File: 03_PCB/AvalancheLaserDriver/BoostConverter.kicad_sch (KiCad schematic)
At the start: 24 parts, among them IC1 LT8365JMSE, SW1 JS202011JAQN

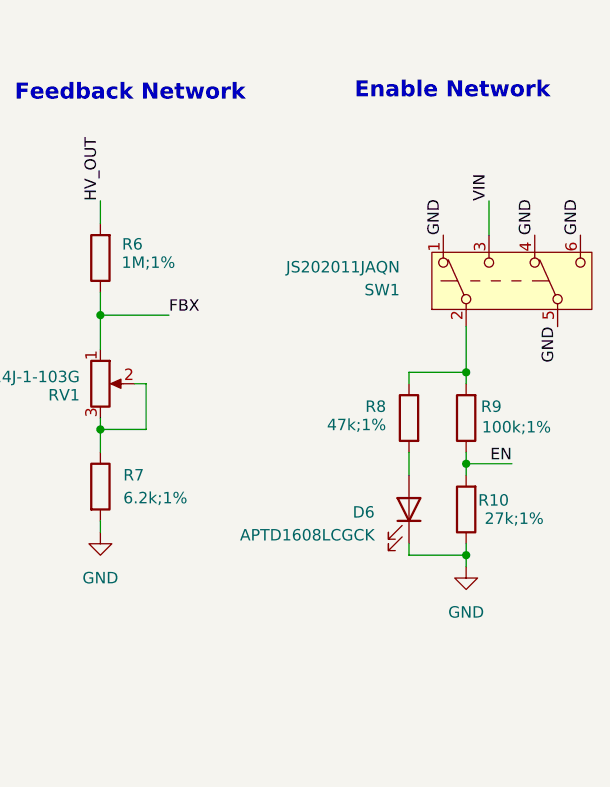
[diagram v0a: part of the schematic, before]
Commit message: feat(pcb): update laser driver circuit after first iteration
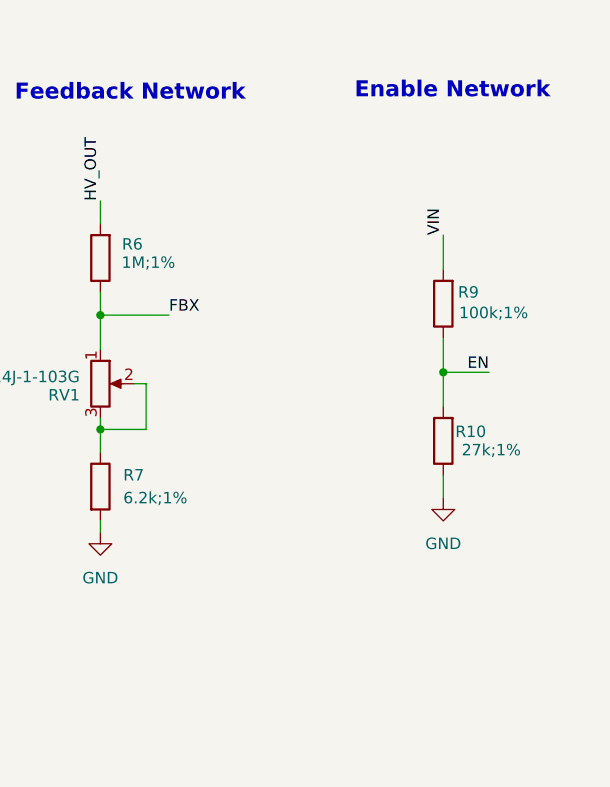
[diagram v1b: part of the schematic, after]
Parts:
- removed D6: APTD1608LCGCK, LED_SMD:LED_0603_1608Metric, symbol Device:LED
- removed R8: 47k;1%, Resistor_SMD:R_0603_1608Metric, symbol Device:R
- removed SW1: JS202011JAQN, Button_Switch_SMD:SW_DPDT_CK_JS202011JCQN, symbol Switch:SW_Push_DPDT
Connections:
- net VIN: now also R9.2
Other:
- moved on the sheet: R10, R9

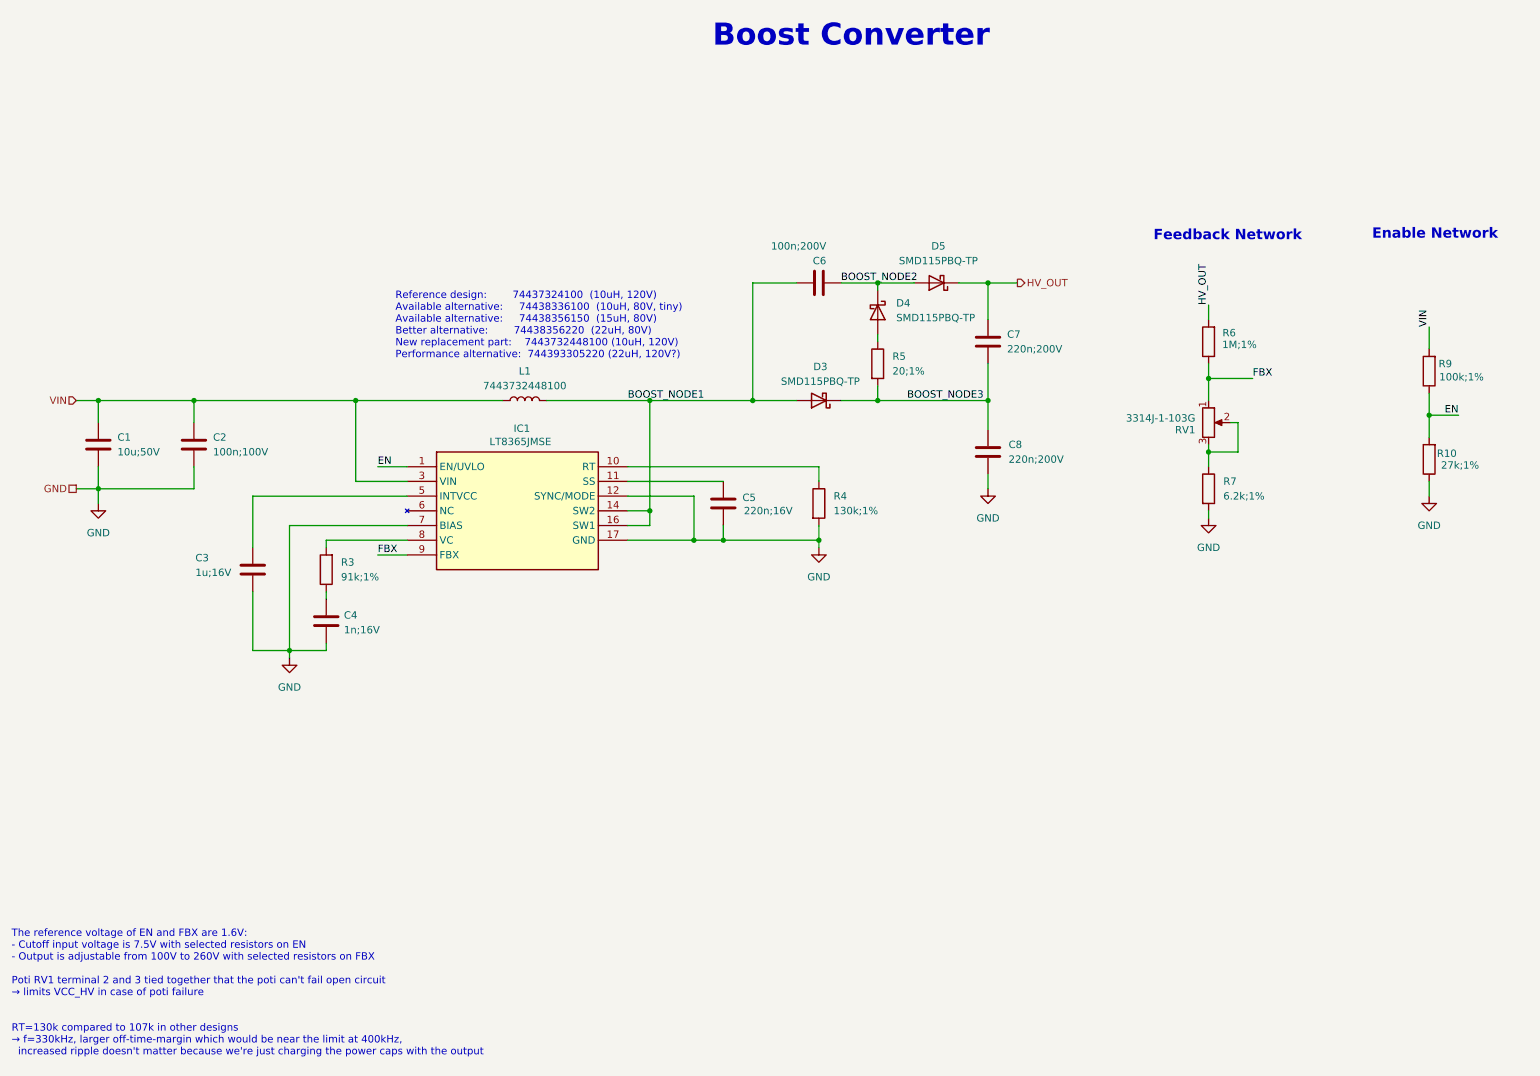
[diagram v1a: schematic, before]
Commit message: feat(pcb): Increase operating voltage to 320V
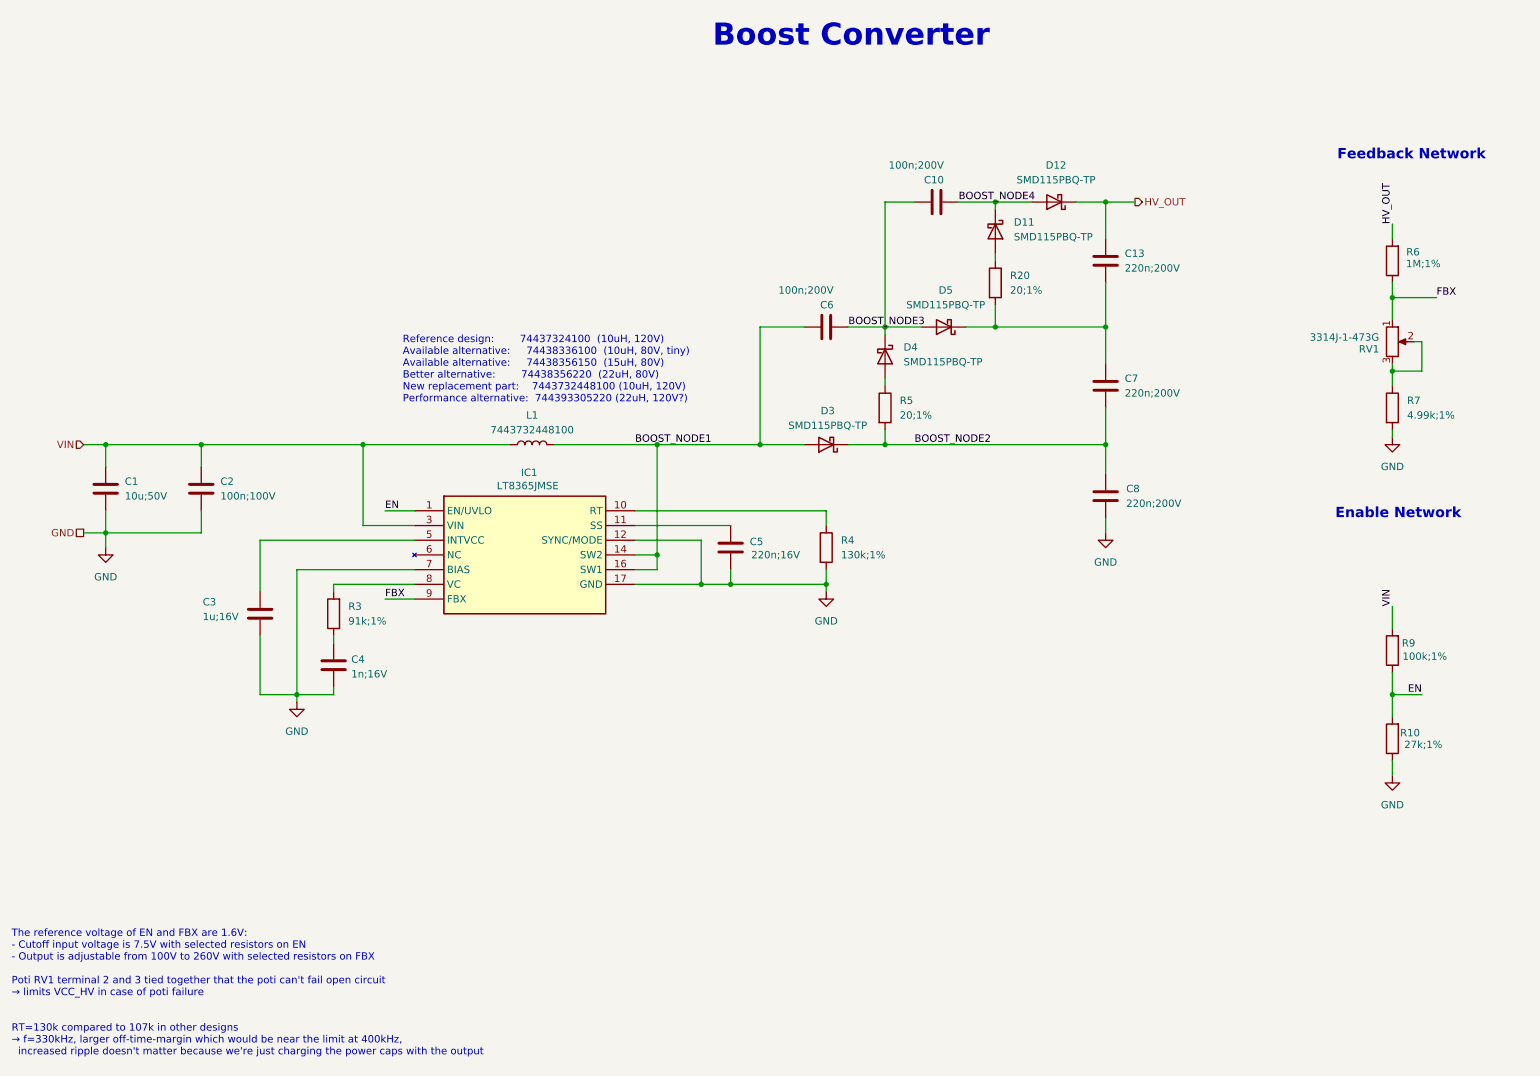
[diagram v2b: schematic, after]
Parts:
- added C10: 100n;200V, Capacitor_SMD:C_0805_2012Metric, symbol Device:C
- added C13: 220n;200V, Capacitor_SMD:C_1206_3216Metric, symbol Device:C
- added D11, D12: SMD115PBQ-TP, CustomFootprints:D_SOD-323HE, symbol Device:D_Schottky
- added R20: 20;1%, Resistor_SMD:R_0603_1608Metric, symbol Device:R
- C6: footprint Capacitor_SMD:C_1206_3216Metric -> Capacitor_SMD:C_0805_2012Metric
- R5: footprint Resistor_SMD:R_0805_2012Metric -> Resistor_SMD:R_0603_1608Metric
- R7: value 6.2k;1% -> 4.99k;1%
- RV1: value 3314J-1-103G -> 3314J-1-473G
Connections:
- net BOOST_NODE2: now also C7.1, C8.2, D3.1 (K), R5.2; no longer C6.2, D4.1 (K), D5.2 (A)
- net BOOST_NODE3: now also C6.2, D4.1 (K), D5.2 (A), C10.1; no longer C7.1, C8.2, D3.1 (K), R5.2
- net HV_OUT: now also C13.2, D12.1 (K); no longer C7.2, D5.1 (K)
- new net: C13.1, C7.2, D5.1 (K), R20.2
- new net: D11.2 (A), R20.1
- new net BOOST_NODE4: C10.2, D11.1 (K), D12.2 (A)
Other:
- moved on the sheet: C1, C2, C3, C4, C5, C6, C7, C8, D3, D4, D5, IC1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

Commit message: feat(pcb): laser driver V0.2 as ordered on 08.04.2026
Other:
- company: (none) -> Hannes Duske
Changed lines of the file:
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@@
 	(title_block
 		(title "DCDC Boost Converter")
+		(date "2026-02-27")
+		(rev "0.2")
+		(company "Hannes Duske")
 	)
 	(text "Enable Network"

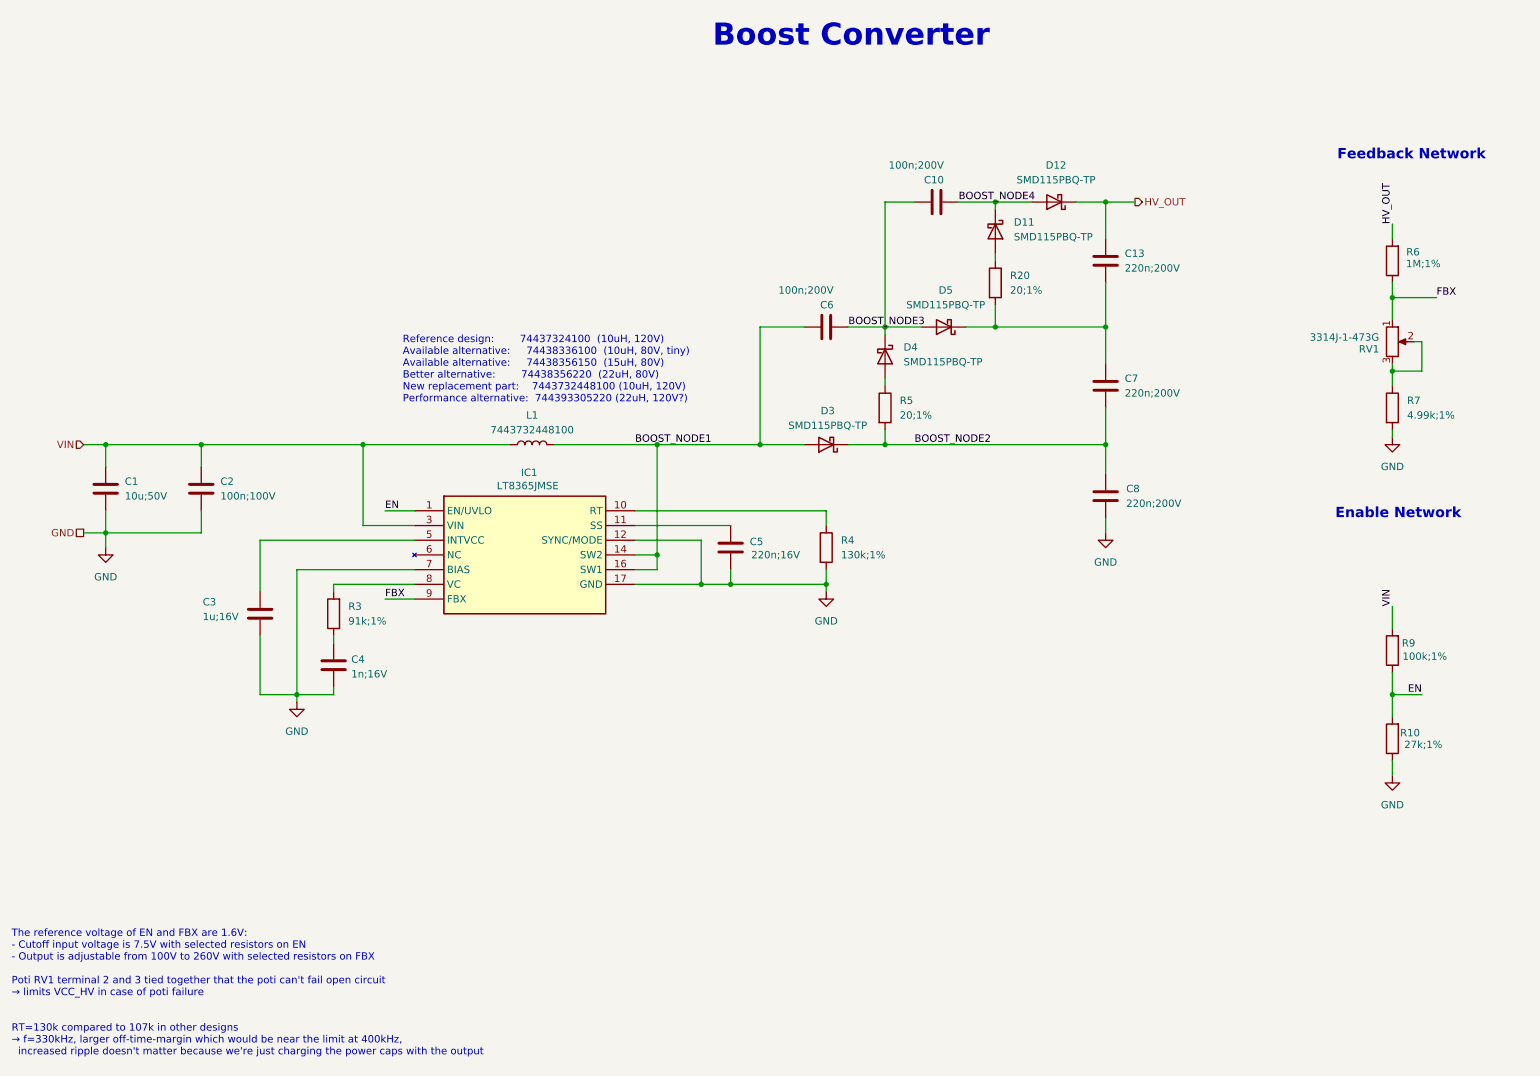
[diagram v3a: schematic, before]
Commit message: chore(pcb): update schematic with tuned component values and update notes
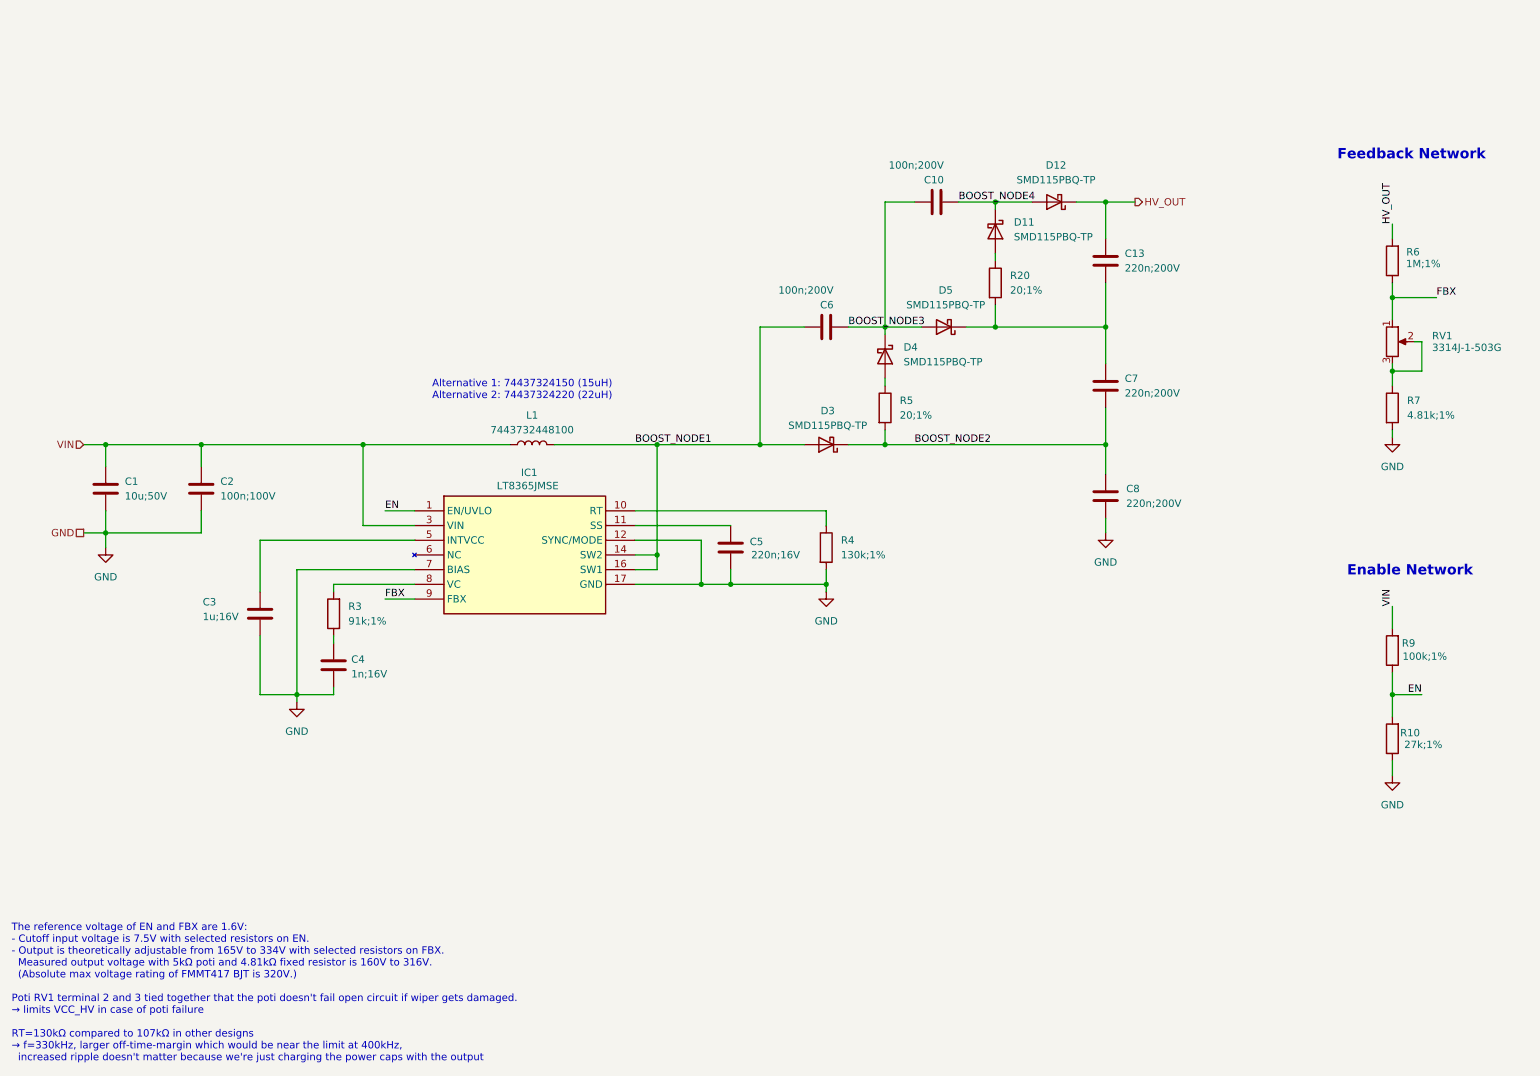
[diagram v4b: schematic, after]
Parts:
- R7: value 4.99k;1% -> 4.81k;1%
- RV1: value 3314J-1-473G -> 3314J-1-503G
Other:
- note added: "Alternative 1: 74437324150 (15uH) Alternative 2: 74437324220 (22uH)"
- note added: "The reference voltage of EN and FBX are 1.6V: - Cutoff input voltage is 7.5V with selected resistors on EN. - Output is theoretically adjustable from 165V to 334V with selected resistors on FBX. Measured output voltage with 5kΩ poti and 4.81kΩ fixed resistor is 160V to 316V. (Absolute max voltage rating of FMMT417 BJT is 320V.) Poti RV1 terminal 2 and 3 tied together that the poti doesn't fail op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"
- note removed: "Boost Converter"
- note removed: "Reference design: 74437324100 (10uH, 120V) Available alternative: 74438336100 (10uH, 80V, tiny) Available alternative: 74438356150 (15uH, 80V) Better alternative: 74438356220 (22uH, 80V) New replacement part: 7443732448100 (10uH, 120V) Performance alternative: 744393305220 (22uH, 120V?)"
- note removed: "The reference voltage of EN and FBX are 1.6V: - Cutoff input voltage is 7.5V with selected resistors on EN - Output is adjustable from 100V to 260V with selected resistors on FBX Poti RV1 terminal 2 and 3 tied together that the poti can't fail open circuit → limits VCC_HV in case of poti failure RT=130k compared to 107k in other designs → f=330kHz, larger off-time-margin which would be near the l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"
- title: DCDC Boost Converter -> Avalanche Laser Driver
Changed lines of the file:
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@@
 	(paper "A4")
 	(title_block
-		(title "DCDC Boost Converter")
+		(title "Avalanche Laser Driver")
 		(date "2026-02-27")
 		(rev "0.2")
@@
 	(text "Enable Network"
 		(exclude_from_sim no)
-		(at 255.016 100.838 0)
+		(at 257.048 110.744 0)
 		(effects
 			(font
@@
 		)
 	)
-	(text "The reference voltage of EN and FBX are 1.6V:\n- Cutoff input voltage is 7.5V with selected resistors on EN\n- Output is adjustable from 100V to 260V with selected resistors on FBX\n\nPoti RV1 terminal 2 and 3 tied together that the poti can't fail open circuit\n→ limits VCC_HV in case of poti failure\n\n\nRT=130k compared to 107k in other designs\n→ f=330kHz, larger off-time-margin which would be near the limit at 400kHz,\n  increased ripple doesn't matter because we're just charging the power caps with the output"
+	(text "The reference voltage of EN and FBX are 1.6V:\n- Cutoff input voltage is 7.5V with selected resistors on EN.\n- Output is theoretically adjustable from 165V to 334V with selected resistors on FBX.\n  Measured output voltage with 5kΩ poti and 4.81kΩ fixed resistor is 160V to 316V.\n  (Absolute max voltage rating of FMMT417 BJT is 320V.)\n\nPoti RV1 terminal 2 and 3 tied together that the poti doesn't fail open circuit if wiper gets damaged.\n→ limits VCC_HV in case of poti failure\n\nRT=130kΩ compared to 107kΩ in other designs\n→ f=330kHz, larger off-time-margin which would be near the limit at 400kHz,\n  increased ripple doesn't matter because we're just charging the power caps with the output"
 		(exclude_from_sim no)
 		(at 15.494 183.642 0)
@@
 		)
 	)
-	(text "Reference design:        74437324100  (10uH, 120V)\nAvailable alternative:     74438336100  (10uH, 80V, tiny)\nAvailable alternative:     74438356150  (15uH, 80V)\nBetter alternative:        74438356220  (22uH, 80V)\nNew replacement part:    7443732448100 (10uH, 120V)\nPerformance alternative:  744393305220 (22uH, 120V?)"
-		(exclude_from_sim no)
-		(at 83.058 70.104 0)
+	(text "Alternative 1: 74437324150 (15uH)\nAlternative 2: 74437324220 (22uH)\n"
+		(exclude_from_sim no)
+		(at 88.138 77.724 0)
 		(effects
 			(font
@@
 			)
 			(justify left top)
-		)
-	)
-	(text "Boost Converter"
-		(exclude_from_sim no)
-		(at 160.528 18.288 0)
-		(effects
-			(font
-				(size 3.81 3.81)
-				(thickness 0.3556)
-				(bold yes)
-			)
 		)
 	)
@@
 			)
 		)
-		(property "Value" "4.99k;1%"
+		(property "Value" "4.81k;1%"
 			(at 256.54 83.8199 0)
 			(effects
@@
 		(dnp no)
 		(property "Reference" "RV1"
-			(at 251.714 72.39 0)
-			(effects
-				(font
-					(size 1.27 1.27)
-				)
-				(justify right)
-			)
-		)
-		(property "Value" "3314J-1-473G"
-			(at 251.714 70.358 0)
-			(effects
-				(font
-					(size 1.27 1.27)
-				)
-				(justify right)
-			)
-		)
+			(at 260.858 70.104 0)
+			(effects
+				(font
+					(size 1.27 1.27)
+				)
+				(justify left)
+			)
+		)
+		(property "Value" "3314J-1-503G"
+			(at 260.858 72.136 0)
+			(effects
+				(font
+					(size 1.27 1.27)
+				)
+				(justify left)
+			)
+		)
